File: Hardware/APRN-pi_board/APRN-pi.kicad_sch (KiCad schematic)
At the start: 2 parts, among them J1 Raspberry_Pi_2_3, U1 DRA818V

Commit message: Add some fluff to schematic
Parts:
- added R1: 100k, Resistor_SMD:R_0805_2012Metric, symbol Device:R
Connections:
- net RXD: now reaches J1.10 (GPIO15/RXD)
- net RXD: now also U1.17 (TXD)
- net GND: now reaches J1.14 (GND)
- net GND: now also J1.20 (GND), J1.25 (GND), J1.30 (GND), J1.34 (GND), J1.39 (GND), J1.6 (GND), J1.9 (GND), U1.10 (GND), U1.9 (GND)
- net +5V: now reaches J1.2 (5V)
- net +5V: now also J1.4 (5V), U1.8 (VBAT), R1.2
- net TXD: now reaches J1.8 (GPIO14/TXD)
- net TXD: now also U1.16 (RXD)
- net at U1.6 (PD): now also R1.1

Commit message: Add more fluff
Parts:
- added H1, H2, H3, H4: MountingHole, MountingHole:MountingHole_2.2mm_M2, symbol Mechanical:MountingHole
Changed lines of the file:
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@@
+    )
+  )
+  (symbol (lib_id "Mechanical:MountingHole") (at 36.83 191.77 0) (unit 1)
+    (in_bom yes) (on_board yes)
+    (property "Reference" "H4" (id 0) (at 39.37 190.4999 0)
+      (effects (font (size 1.27 1.27)) (justify left))
+    )
+    (property "Value" "MountingHole" (id 1) (at 30.48 194.31 0)
+      (effects (font (size 1.27 1.27)) (justify left))
+    )
+    (property "Footprint" "MountingHole:MountingHole_2.2mm_M2" (id 2) (at 36.83 191.77 0)
+      (effects (font (size 1.27 1.27)) hide)
+    )
+    (property "Datasheet" "~" (id 3) (at 36.83 191.77 0)
+      (effects (font (size 1.27 1.27)) hide)
     )
   )
@@
     )
     (pin "1")
+  )
+  (symbol (lib_id "Mechanical:MountingHole") (at 21.59 191.77 0) (unit 1)
+    (in_bom yes) (on_board yes)
+    (property "Reference" "H3" (id 0) (at 24.13 190.4999 0)
+      (effects (font (size 1.27 1.27)) (justify left))
+    )
+    (property "Value" "MountingHole" (id 1) (at 15.24 194.31 0)
+      (effects (font (size 1.27 1.27)) (justify left))
+    )
+    (property "Footprint" "MountingHole:MountingHole_2.2mm_M2" (id 2) (at 21.59 191.77 0)
+      (effects (font (size 1.27 1.27)) hide)
+    )
+    (property "Datasheet" "~" (id 3) (at 21.59 191.77 0)
+      (effects (font (size 1.27 1.27)) hide)
+    )
   )
   (symbol (lib_id "Device:R") (at 265.43 50.8 90) (unit 1)
@@
     (pin "1")
   )
+  (symbol (lib_id "Mechanical:MountingHole") (at 21.59 184.15 0) (unit 1)
+    (in_bom yes) (on_board yes)
+    (property "Reference" "H1" (id 0) (at 24.13 182.8799 0)
+      (effects (font (size 1.27 1.27)) (justify left))
+    )
+    (property "Value" "MountingHole" (id 1) (at 15.24 187.96 0)
+      (effects (font (size 1.27 1.27)) (justify left))
+    )
+    (property "Footprint" "MountingHole:MountingHole_2.2mm_M2" (id 2) (at 21.59 184.15 0)
+      (effects (font (size 1.27 1.27)) hide)
+    )
+    (property "Datasheet" "~" (id 3) (at 21.59 184.15 0)
+      (effects (font (size 1.27 1.27)) hide)
+    )
+  )
+  (symbol (lib_id "Mechanical:MountingHole") (at 36.83 184.15 0) (unit 1)
+    (in_bom yes) (on_board yes)
+    (property "Reference" "H2" (id 0) (at 39.37 182.8799 0)
+      (effects (font (size 1.27 1.27)) (justify left))
+    )
+    (property "Value" "MountingHole" (id 1) (at 30.48 187.96 0)
+      (effects (font (size 1.27 1.27)) (justify left))
+    )
+    (property "Footprint" "MountingHole:MountingHole_2.2mm_M2" (id 2) (at 36.83 184.15 0)
+      (effects (font (size 1.27 1.27)) hide)
+    )
+    (property "Datasheet" "~" (id 3) (at 36.83 184.15 0)
+      (effects (font (size 1.27 1.27)) hide)
+    )
+  )
   (symbol (lib_id "KenwoodFox:DRA818V") (at 240.03 44.45 0) (unit 1)
     (in_bom yes) (on_board yes) (fields_autoplaced)
@@
       (reference "#PWR0104") (unit 1) (value "+5V") (footprint "")
     )
+    (path "/85c3f4c6-6a16-4336-a601-68606d8db4b4"
+      (reference "H1") (unit 1) (value "MountingHole") (footprint "MountingHole:MountingHole_2.2mm_M2")
+    )
+    (path "/91b0ff9a-a35c-4fec-89cf-75f03e9ac5f6"
+      (reference "H2") (unit 1) (value "MountingHole") (footprint "MountingHole:MountingHole_2.2mm_M2")
+    )
+    (path "/22b49795-d138-447a-8a67-2f87ad0d4bd4"
+      (reference "H3") (unit 1) (value "MountingHole") (footprint "MountingHole:MountingHole_2.2mm_M2")
+    )
+    (path "/0abad01c-8cfb-4cd7-9f2d-5ad9e9479b46"
+      (reference "H4") (unit 1) (value "MountingHole") (footprint "MountingHole:MountingHole_2.2mm_M2")
+    )
     (path "/3f3bf25c-fe77-4cf4-b69b-53b67dff8a67"

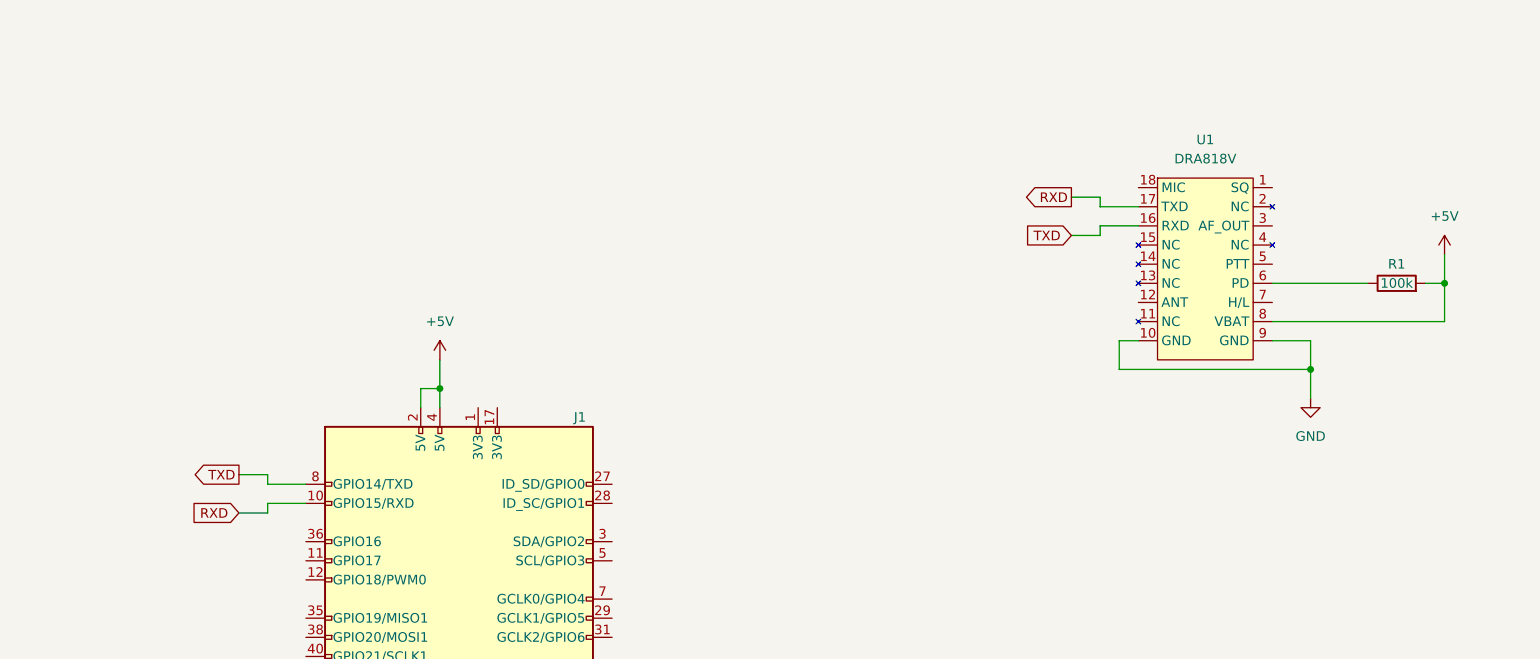
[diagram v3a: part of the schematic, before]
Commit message: Add RF components into schematic
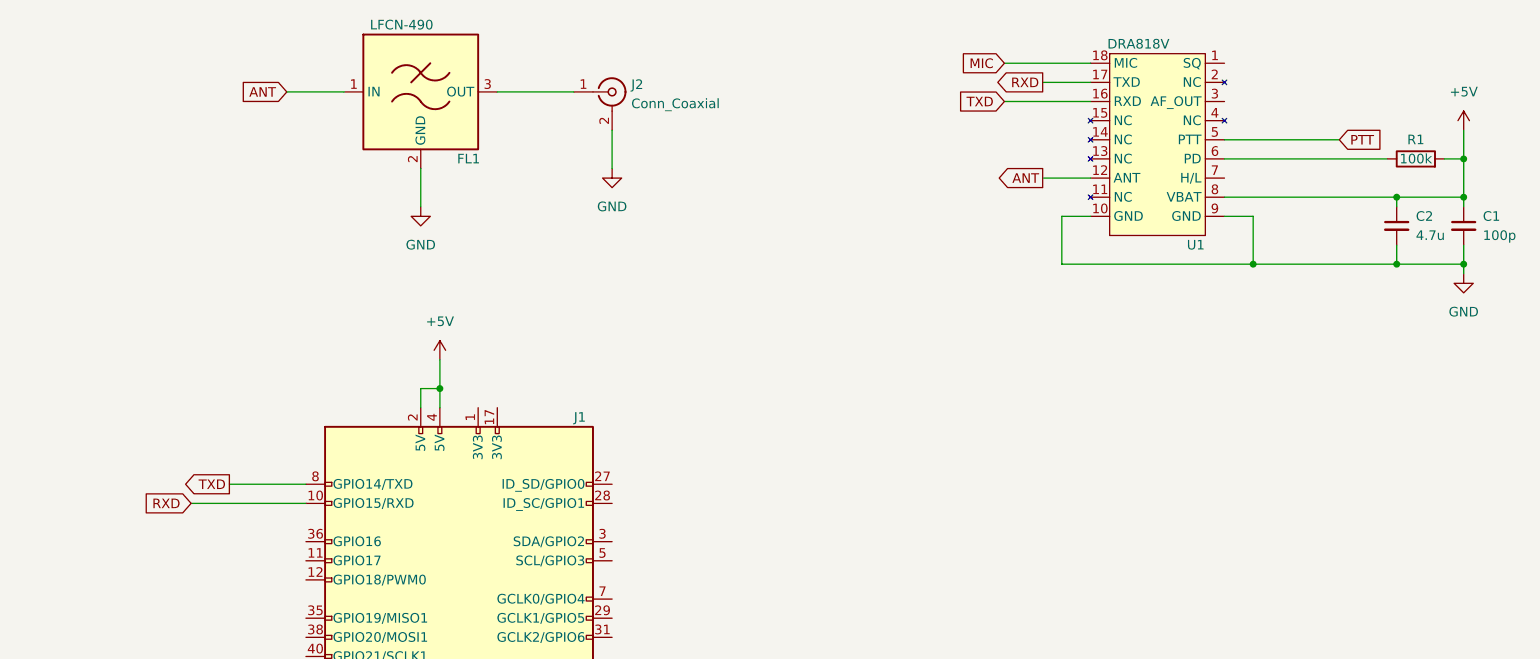
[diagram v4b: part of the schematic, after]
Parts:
- added C1: 100p, Capacitor_SMD:C_0201_0603Metric, symbol Device:C_Small
- added C2: 4.7u, Capacitor_SMD:C_0201_0603Metric, symbol Device:C_Small
- added FL1: LFCN-490, Filter:Filter_Mini-Circuits_FV1206, symbol RF_Filter:LFCN-490
- added J2: Conn_Coaxial, Connector_Coaxial:SMA_Amphenol_132291_Vertical, symbol Connector:Conn_Coaxial
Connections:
- net +5V: now also C1.1, C2.1
- net GND: now also C1.2, C2.2, FL1.2 (GND), FL1.4 (GND), J2.2 (Ext)
- net ANT: now reaches U1.12 (ANT)
- net ANT: now also FL1.1 (IN)
- net MIC: now reaches U1.18 (MIC)
- net PTT: now reaches U1.5 (PTT)
- new net: FL1.3 (OUT), J2.1 (In)
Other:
- moved on the sheet: R1, U1

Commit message: Bump to new logo and add logo
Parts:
- added L1: KITSUNE_LOGO, KenwoodFox:KITSUNE_LOGO, symbol KenwoodFox:KITSUNE_LOGO
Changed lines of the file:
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@@
+    )
+  )
+  (symbol (lib_id "KenwoodFox:KITSUNE_LOGO") (at 13.97 176.53 0) (unit 1)
+    (in_bom yes) (on_board yes) (fields_autoplaced)
+    (property "Reference" "L1" (id 0) (at 15.24 175.2599 0)
+      (effects (font (size 1.27 1.27)) (justify left))
+    )
+    (property "Value" "KITSUNE_LOGO" (id 1) (at 15.24 177.7999 0)
+      (effects (font (size 1.27 1.27)) (justify left))
+    )
+    (property "Footprint" "KenwoodFox:KITSUNE_LOGO" (id 2) (at 13.97 176.53 0)
+      (effects (font (size 1.27 1.27)) hide)
+    )
+    (property "Datasheet" "" (id 3) (at 13.97 176.53 0)
+      (effects (font (size 1.27 1.27)) hide)
     )
   )
@@
       (reference "J2") (unit 1) (value "Conn_Coaxial") (footprint "Connector_Coaxial:SMA_Amphenol_132291_Vertical")
     )
+    (path "/934fbbb7-68d4-48b2-b966-8b80b47dd229"
+      (reference "L1") (unit 1) (value "KITSUNE_LOGO") (footprint "KenwoodFox:KITSUNE_LOGO")
+    )
     (path "/3b7d4af7-36a9-44c1-bf8f-a8095fb08dc6"

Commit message: Clean up naming
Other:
- company: (none) -> Kitsune Scientific
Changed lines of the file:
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@@
     (date "${ISSUE}")
     (rev "${REVISION}")
-    (comment 4 "${FULL_REVISION}")
+    (company "Kitsune Scientific")
+    (comment 4 "Release: ${FULL_REVISION}")
   )
   (junction (at 148.59 135.89) (diameter 0) (color 0 0 0 0)

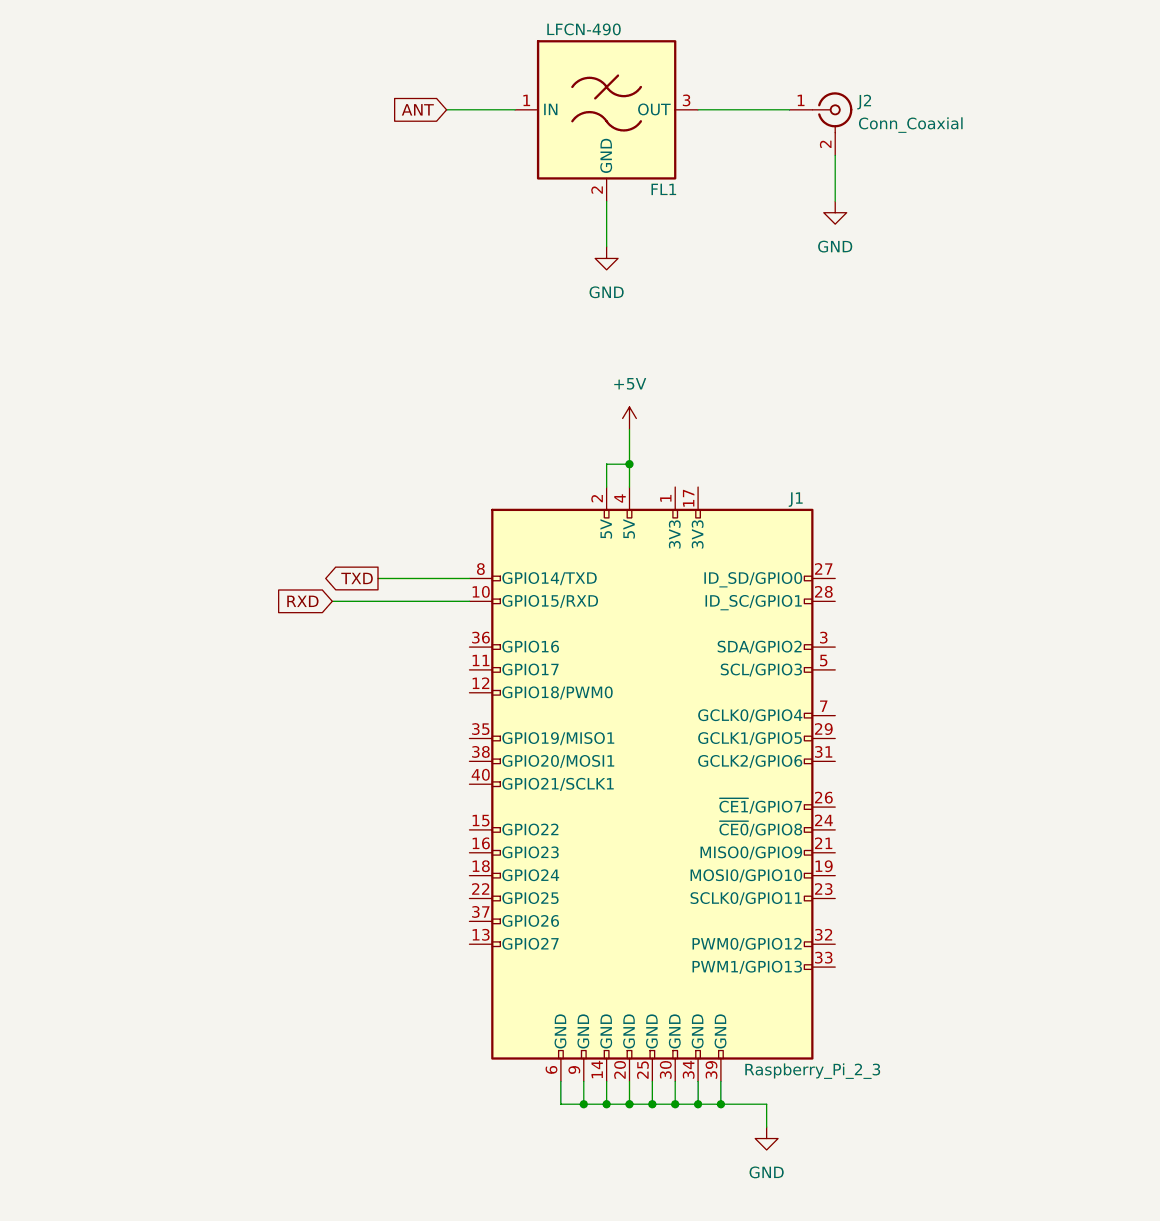
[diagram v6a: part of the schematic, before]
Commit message: Fix RF stuff with help from @Gandalf#1068
Co-Authored By: @ka2qfx
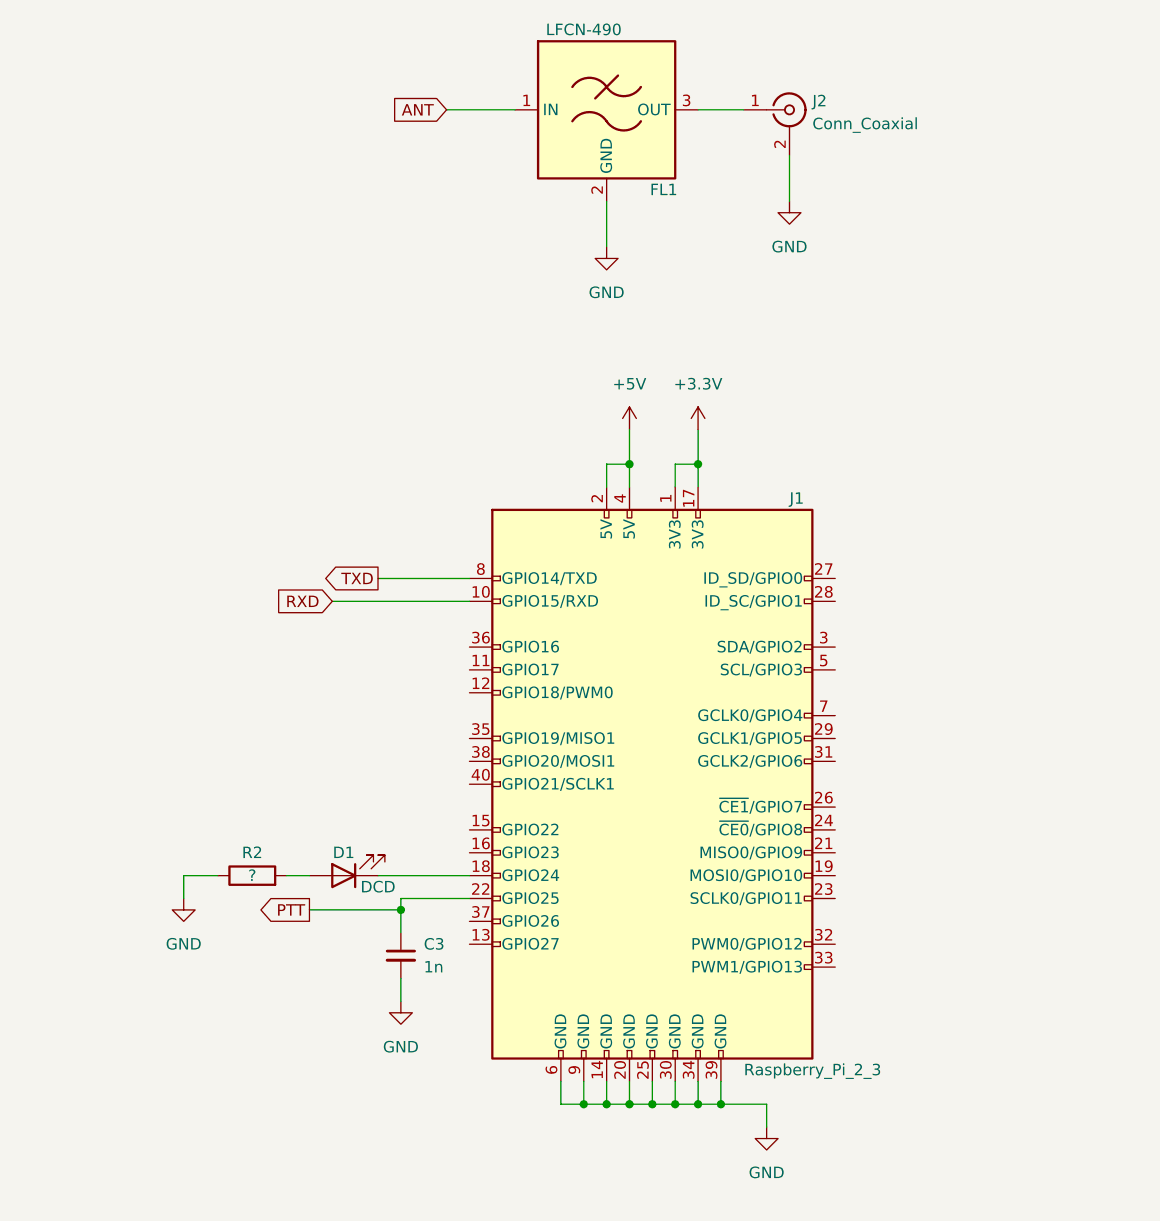
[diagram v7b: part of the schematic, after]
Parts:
- added C3: 1n, Capacitor_SMD:C_0805_2012Metric, symbol Device:C_Small
- added D1: DCD, LED_SMD:LED_0603_1608Metric, symbol Device:LED
- added R2: ?, Resistor_SMD:R_0805_2012Metric, symbol Device:R
- C1, C2: footprint Capacitor_SMD:C_0201_0603Metric -> Capacitor_SMD:C_0805_2012Metric
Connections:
- net GND: now also C3.2, R2.1
- net PTT: now also J1.22 (GPIO25), C3.1
- net +3V3: now reaches J1.1 (3V3)
- net +3V3: now also J1.17 (3V3)
- net at J1.18 (GPIO24): now also D1.1 (K)
- new net: D1.2 (A), R2.2
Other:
- moved on the sheet: J2

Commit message: Even more fixups, thx!
Co-Authored By: @ka2qfx
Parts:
- added D1: RX, LED_SMD:LED_0603_1608Metric, symbol Device:LED
- added D3: TX, LED_SMD:LED_0603_1608Metric, symbol Device:LED
- added J3: Amplifier Jumper, Connector_PinHeader_2.54mm:PinHeader_1x03_P2.54mm_Vertical, symbol Connector:Conn_01x03_Male
- added Q1: 2N3906, Package_TO_SOT_THT:TO-92_Inline, symbol Transistor_BJT:2N3906
- added R1, R3: 180, Resistor_SMD:R_0805_2012Metric, symbol Device:R
- R2: value ? -> 180
- renumbered D1 to D2, R1 to R4
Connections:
- net +3V3: now also R2.1, Q1.1 (E), R1.1
- net GND: now also J3.2 (Pin_2); no longer J1.14 (GND), J1.20 (GND), J1.30 (GND), J1.34 (GND), J1.6 (GND), R2.1
- net PTT: now also D3.1 (K)
- net SQL: now reaches U1.1 (SQ)
- net SQL: now also D1.1 (K)
- new net: J3.1 (Pin_1), Q1.3 (C)
- new net: D1.2 (A), R1.2
- new net: Q1.2 (B), R3.1
- new net: D3.2 (A), R3.2
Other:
- moved on the sheet: C3, D2, R2
